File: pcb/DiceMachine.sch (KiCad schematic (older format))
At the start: 12 parts, among them J1 Conn_01x02, J2 Conn_01x02, J3 Conn_01x02, U1 arduino_mini

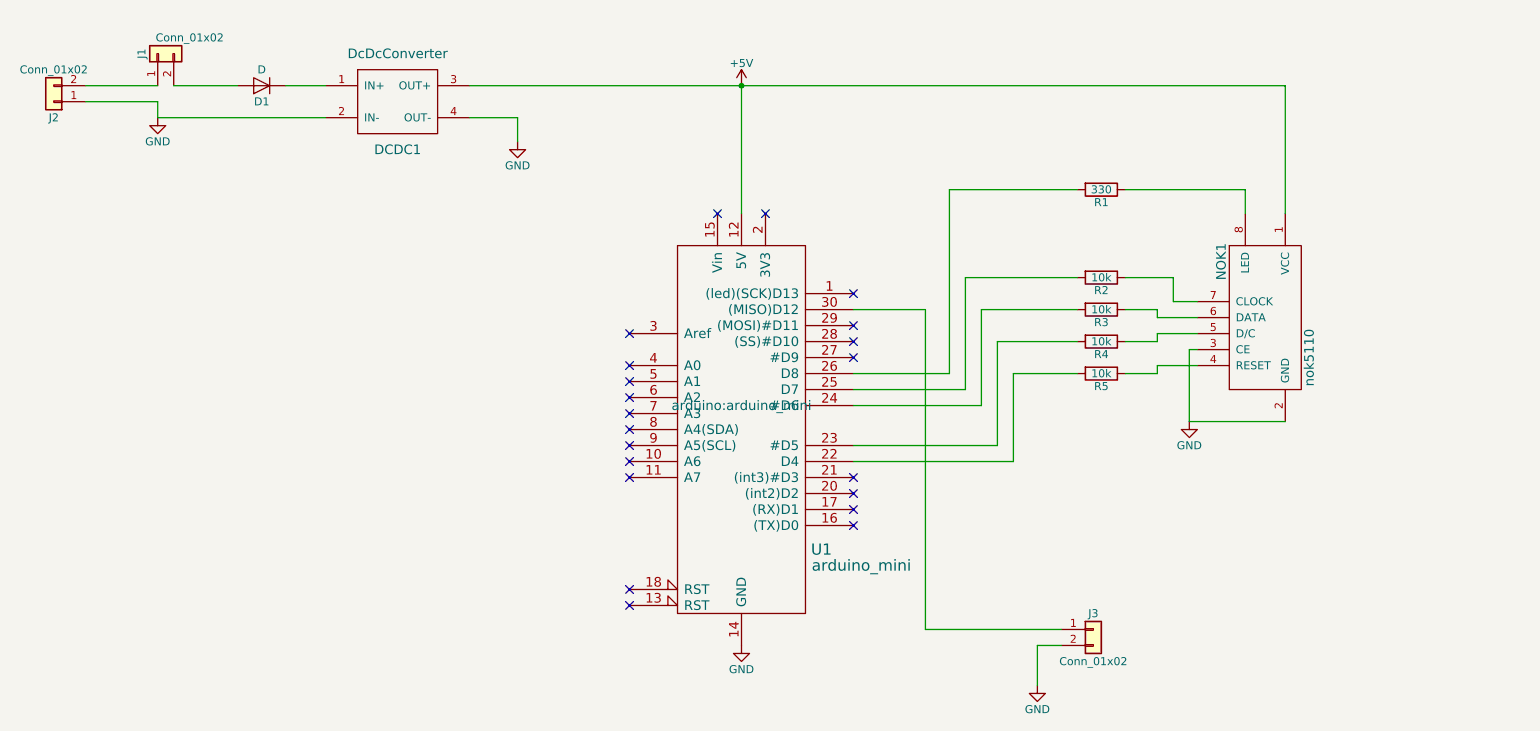
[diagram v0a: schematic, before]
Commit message: added level shifter to PCB
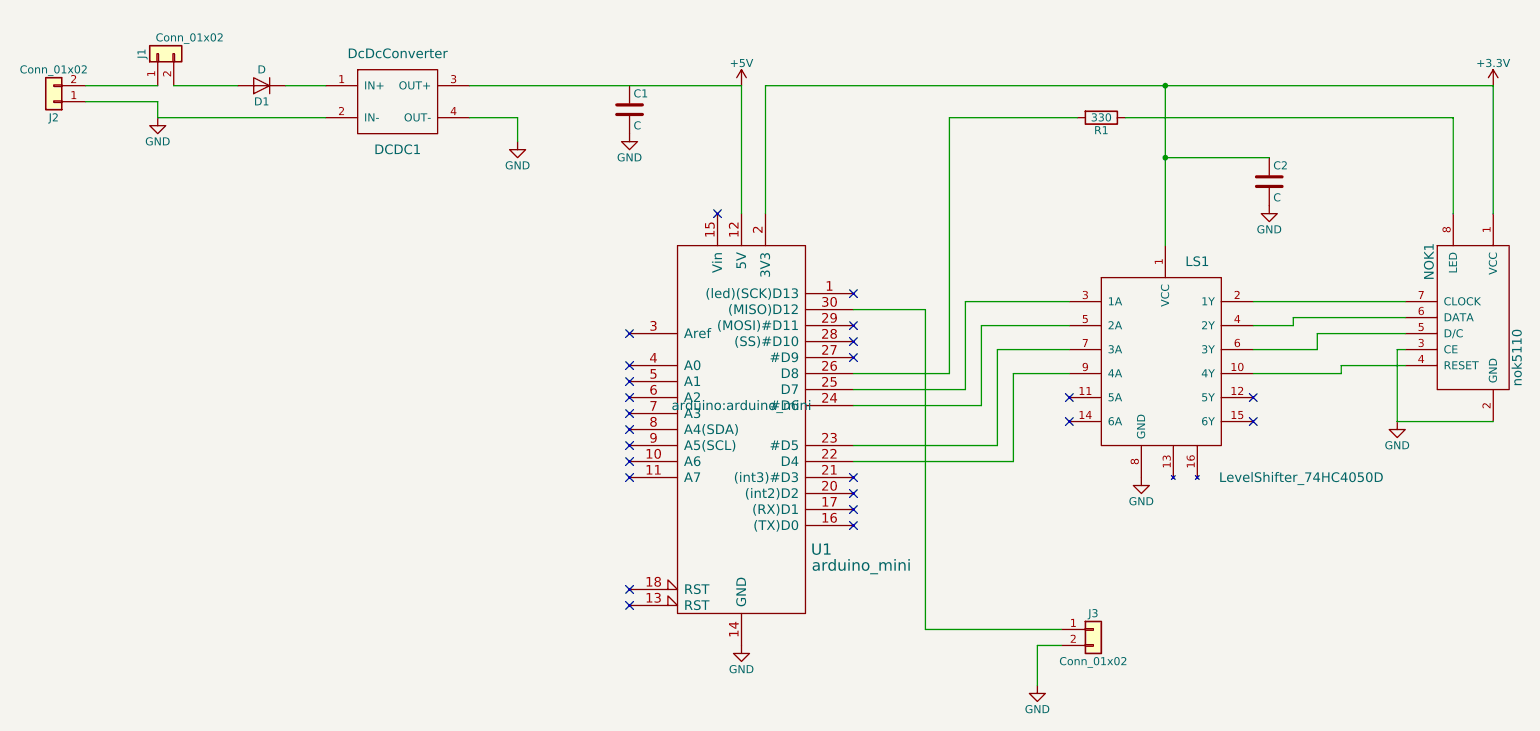
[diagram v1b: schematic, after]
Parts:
- removed R2, R3, R4, R5: 10k, Resistors_ThroughHole:Resistor_Horizontal_RM7mm, symbol R
- added C1, C2: C, Capacitors_SMD:C_1206_HandSoldering, symbol C
- added LS1: LevelShifter_74HC4050D, Housings_SSOP:SOP-16_4.4x10.4mm_Pitch1.27mm, symbol LevelShifter_74HC4050D
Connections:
- net +5V: no longer NOK1.1 (VCC)
- net GND: now also C1.2, C2.2, LS1.8 (GND)
- net +3V3: now reaches U1.2 (3V3)
- net +3V3: now also NOK1.1 (VCC), C2.1, LS1.1 (VCC)
- net at U1.22 (D4): now also LS1.9 (4A)
- net at U1.23 (#D5): now also LS1.7 (3A)
- net at U1.24 (#D6): now also LS1.5 (2A)
- net at U1.25 (D7): now also LS1.3 (1A)
- net at NOK1.7 (CLOCK): now also LS1.2 (1Y)
- net at NOK1.6 (DATA): now also LS1.4 (2Y)
- net at NOK1.5 (D/C): now also LS1.6 (3Y)
- net at NOK1.4 (RESET): now also LS1.10 (4Y)
- no-connect marks 21 -> 24
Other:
- moved on the sheet: NOK1, R1
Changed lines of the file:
@@
 LIBS:arduino
 LIBS:nok5110
+LIBS:levelshifter_74hc4050d
 LIBS:DiceMachine-cache
 EELAYER 25 0
@@
 $EndComp
 $Comp
-L R R2
-U 1 1 59ECDA35
-P 7950 2600
-F 0 "R2" V 8030 2600 50  0000 C CNN
-F 1 "10k" V 7950 2600 50  0000 C CNN
-F 2 "Resistors_ThroughHole:Resistor_Horizontal_RM7mm" V 7880 2600 50  0001 C CNN
-F 3 "" H 7950 2600 50  0001 C CNN
-	1    7950 2600
-	0    1    1    0
-$EndComp
-$Comp
-L R R3
-U 1 1 59ECDAEE
-P 7950 2800
-F 0 "R3" V 8030 2800 50  0000 C CNN
-F 1 "10k" V 7950 2800 50  0000 C CNN
-F 2 "Resistors_ThroughHole:Resistor_Horizontal_RM7mm" V 7880 2800 50  0001 C CNN
-F 3 "" H 7950 2800 50  0001 C CNN
-	1    7950 2800
-	0    1    1    0
-$EndComp
-$Comp
-L R R4
-U 1 1 59ECDC0A
-P 7950 3000
-F 0 "R4" V 8030 3000 50  0000 C CNN
-F 1 "10k" V 7950 3000 50  0000 C CNN
-F 2 "Resistors_ThroughHole:Resistor_Horizontal_RM7mm" V 7880 3000 50  0001 C CNN
-F 3 "" H 7950 3000 50  0001 C CNN
-	1    7950 3000
-	0    1    1    0
-$EndComp
-$Comp
-L R R5
-U 1 1 59ECDC61
-P 7950 3200
-F 0 "R5" V 8030 3200 50  0000 C CNN
-F 1 "10k" V 7950 3200 50  0000 C CNN
-F 2 "Resistors_ThroughHole:Resistor_Horizontal_RM7mm" V 7880 3200 50  0001 C CNN
-F 3 "" H 7950 3200 50  0001 C CNN
-	1    7950 3200
-	0    1    1    0
-$EndComp
-$Comp
 L R R1
 U 1 1 59ECDCA8
-P 7950 2050
-F 0 "R1" V 8030 2050 50  0000 C CNN
-F 1 "330" V 7950 2050 50  0000 C CNN
-F 2 "Resistors_ThroughHole:Resistor_Horizontal_RM7mm" V 7880 2050 50  0001 C CNN
-F 3 "" H 7950 2050 50  0001 C CNN
-	1    7950 2050
+P 7950 1600
+F 0 "R1" V 8030 1600 50  0000 C CNN
+F 1 "330" V 7950 1600 50  0000 C CNN
+F 2 "Resistors_ThroughHole:Resistor_Horizontal_RM7mm" V 7880 1600 50  0001 C CNN
+F 3 "" H 7950 1600 50  0001 C CNN
+	1    7950 1600
 	0    1    1    0
 $EndComp
 Wire Wire Line
-	5700 2200 5700 1400
-Wire Wire Line
-	4000 1400 9100 1400
-Wire Wire Line
-	8850 2050 8850 2200
-Wire Wire Line
-	8100 2600 8400 2600
-Wire Wire Line
-	8400 2600 8400 2750
-Wire Wire Line
-	8400 2750 8550 2750
-Wire Wire Line
-	8300 2850 8550 2850
-Wire Wire Line
-	8300 2950 8550 2950
-Wire Wire Line
-	8550 3050 8500 3050
-Wire Wire Line
-	8500 3050 8500 3500
-Wire Wire Line
-	8500 3500 9100 3500
-$Comp
-L GND #PWR01
+	9850 3050 9800 3050
+Wire Wire Line
+	9800 3050 9800 3500
+Wire Wire Line
+	9800 3500 10400 3500
+$Comp
+L GND #PWR7
 U 1 1 59ECE495
-P 8500 3500
-F 0 "#PWR01" H 8500 3250 50  0001 C CNN
-F 1 "GND" H 8500 3350 50  0000 C CNN
-F 2 "" H 8500 3500 50  0001 C CNN
-F 3 "" H 8500 3500 50  0001 C CNN
-	1    8500 3500
-	1    0    0    -1
-$EndComp
-Wire Wire Line
-	8100 3200 8300 3200
-Wire Wire Line
-	8300 3200 8300 3150
-Wire Wire Line
-	8300 3150 8550 3150
-Wire Wire Line
-	8300 2950 8300 3000
-Wire Wire Line
-	8300 3000 8100 3000
-Wire Wire Line
-	8300 2850 8300 2800
-Wire Wire Line
-	8300 2800 8100 2800
-Wire Wire Line
-	8100 2050 8850 2050
-Wire Wire Line
-	9100 1400 9100 2200
+P 9800 3500
+F 0 "#PWR7" H 9800 3250 50  0001 C CNN
+F 1 "GND" H 9800 3350 50  0000 C CNN
+F 2 "" H 9800 3500 50  0001 C CNN
+F 3 "" H 9800 3500 50  0001 C CNN
+	1    9800 3500
+	1    0    0    -1
+$EndComp
+Wire Wire Line
+	8100 1600 10150 1600
 Wire Wire Line
 	6400 3200 7000 3200
 Wire Wire Line
-	7000 3200 7000 2050
-Wire Wire Line
-	7000 2050 7800 2050
+	7000 3200 7000 1600
+Wire Wire Line
+	7000 1600 7800 1600
 Wire Wire Line
 	6400 3300 7100 3300
 Wire Wire Line
-	7100 3300 7100 2600
-Wire Wire Line
-	7100 2600 7800 2600
+	7100 3300 7100 2750
 Wire Wire Line
 	6400 3400 7200 3400
 Wire Wire Line
-	7200 3400 7200 2800
-Wire Wire Line
-	7200 2800 7800 2800
+	7200 3400 7200 2900
 Wire Wire Line
 	6400 3650 7300 3650
 Wire Wire Line
-	7300 3650 7300 3000
-Wire Wire Line
-	7300 3000 7800 3000
+	7300 3650 7300 3050
 Wire Wire Line
 	6400 3750 7400 3750
@@
 	7400 3750 7400 3200
 Wire Wire Line
-	7400 3200 7800 3200
-Wire Wire Line
 	6400 2800 6850 2800
 Wire Wire Line
@@
 	7550 4900 7550 5150
 $Comp
-L GND #PWR02
+L GND #PWR10
 U 1 1 59ECEB05
 P 7550 5150
-F 0 "#PWR02" H 7550 4900 50  0001 C CNN
+F 0 "#PWR10" H 7550 4900 50  0001 C CNN
 F 1 "GND" H 7550 5000 50  0000 C CNN
 F 2 "" H 7550 5150 50  0001 C CNN
@@
 	1    0    0    -1
 $EndComp
-Connection ~ 5700 1400
 Wire Wire Line
 	4000 1600 4300 1600
@@
 	4300 1600 4300 1750
 $Comp
-L GND #PWR03
+L GND #PWR5
 U 1 1 59ECECE3
 P 4300 1750
-F 0 "#PWR03" H 4300 1500 50  0001 C CNN
+F 0 "#PWR5" H 4300 1500 50  0001 C CNN
 F 1 "GND" H 4300 1600 50  0000 C CNN
 F 2 "" H 4300 1750 50  0001 C CNN
@@
 	2050 1600 3100 1600
 $Comp
-L GND #PWR04
+L GND #PWR9
 U 1 1 59ECEF76
 P 5700 4900
-F 0 "#PWR04" H 5700 4650 50  0001 C CNN
+F 0 "#PWR9" H 5700 4650 50  0001 C CNN
 F 1 "GND" H 5700 4750 50  0000 C CNN
 F 2 "" H 5700 4900 50  0001 C CNN
@@
 NoConn ~ 5000 3850
 NoConn ~ 5550 2200
-NoConn ~ 5850 2200
 $Comp
 L nok5110 NOK1
 U 1 1 59ECF53D
-P 9000 2850
-F 0 "NOK1" V 8700 3200 60  0000 C CNN
-F 1 "nok5110" V 9250 2600 60  0000 C CNN
-F 2 "Pin_Headers:Pin_Header_Straight_1x08" H 8900 3600 60  0001 C CNN
-F 3 "" H 8900 3600 60  0001 C CNN
-	1    9000 2850
-	1    0    0    -1
-$EndComp
-$Comp
-L +5V #PWR?
+P 10300 2850
+F 0 "NOK1" V 10000 3200 60  0000 C CNN
+F 1 "nok5110" V 10550 2600 60  0000 C CNN
+F 2 "Pin_Headers:Pin_Header_Straight_1x08" H 10200 3600 60  0001 C CNN
+F 3 "" H 10200 3600 60  0001 C CNN
+	1    10300 2850
+	1    0    0    -1
+$EndComp
+$Comp
+L +5V #PWR1
 U 1 1 59ECF8EA
 P 5700 1400
-F 0 "#PWR?" H 5700 1250 50  0001 C CNN
+F 0 "#PWR1" H 5700 1250 50  0001 C CNN
 F 1 "+5V" H 5700 1540 50  0000 C CNN
 F 2 "" H 5700 1400 50  0001 C CNN
@@
 $EndComp
 $Comp
-L GND #PWR?
+L GND #PWR3
 U 1 1 59ECFAC3
 P 2050 1600
-F 0 "#PWR?" H 2050 1350 50  0001 C CNN
+F 0 "#PWR3" H 2050 1350 50  0001 C CNN
 F 1 "GND" H 2050 1450 50  0000 C CNN
 F 2 "" H 2050 1600 50  0001 C CNN
@@
 	1    0    0    -1
 $EndComp
+$Comp
+L LevelShifter_74HC4050D LS1
+U 1 1 59FB6E3B
+P 8350 3050
+F 0 "LS1" H 8550 3600 60  0000 C CNN
+F 1 "LevelShifter_74HC4050D" H 9200 2250 60  0000 C CNN
+F 2 "Housings_SSOP:SOP-16_4.4x10.4mm_Pitch1.27mm" H 8350 3050 60  0001 C CNN
+F 3 "" H 8350 3050 60  0000 C CNN
+	1    8350 3050
+	1    0    0    -1
+$EndComp
+Wire Wire Line
+	5700 2200 5700 1400
+Wire Wire Line
+	5700 1400 4000 1400
+Wire Wire Line
+	5850 2200 5850 1400
+Wire Wire Line
+	5850 1400 10400 1400
+Wire Wire Line
+	10400 1400 10400 2200
+$Comp
+L +3.3V #PWR2
+U 1 1 59FB7034
+P 10400 1400
+F 0 "#PWR2" H 10400 1250 50  0001 C CNN
+F 1 "+3.3V" H 10400 1540 50  0000 C CNN
+F 2 "" H 10400 1400 50  0001 C CNN
+F 3 "" H 10400 1400 50  0001 C CNN
+	1    10400 1400
+	1    0    0    -1
+$EndComp
+Wire Wire Line
+	10150 1600 10150 2200
+$Comp
+L GND #PWR8
+U 1 1 59FB736B
+P 8200 3850
+F 0 "#PWR8" H 8200 3600 50  0001 C CNN
+F 1 "GND" H 8200 3700 50  0000 C CNN
+F 2 "" H 8200 3850 50  0001 C CNN
+F 3 "" H 8200 3850 50  0001 C CNN
+	1    8200 3850
+	1    0    0    -1
+$EndComp
+Wire Wire Line
+	8900 2750 9850 2750
+Wire Wire Line
+	7100 2750 7750 2750
+Wire Wire Line
+	7200 2900 7750 2900
+Wire Wire Line
+	8900 2900 9150 2900
+Wire Wire Line
+	9150 2900 9150 2850
+Wire Wire Line
+	9150 2850 9850 2850
+Wire Wire Line
+	7300 3050 7750 3050
+Wire Wire Line
+	8900 3050 9300 3050
+Wire Wire Line
+	9300 3050 9300 2950
+Wire Wire Line
+	9300 2950 9850 2950
+Wire Wire Line
+	7400 3200 7750 3200
+Wire Wire Line
+	8900 3200 9450 3200
+Wire Wire Line
+	9450 3200 9450 3150
+Wire Wire Line
+	9450 3150 9850 3150
+NoConn ~ 8900 3350
+NoConn ~ 8900 3500
+NoConn ~ 7750 3350
+NoConn ~ 7750 3500
+Wire Wire Line
+	8350 2400 8350 1400
+Connection ~ 8350 1400
+$Comp
+L C C2
+U 1 1 59FB7999
+P 9000 2000
+F 0 "C2" H 9025 2100 50  0000 L CNN
+F 1 "C" H 9025 1900 50  0000 L CNN
+F 2 "Capacitors_SMD:C_1206_HandSoldering" H 9038 1850 50  0001 C CNN
+F 3 "" H 9000 2000 50  0001 C CNN
+	1    9000 2000
+	1    0    0    -1
+$EndComp
+$Comp
+L GND #PWR6
+U 1 1 59FB7A2C
+P 9000 2150
+F 0 "#PWR6" H 9000 1900 50  0001 C CNN
+F 1 "GND" H 9000 2000 50  0000 C CNN
+F 2 "" H 9000 2150 50  0001 C CNN
+F 3 "" H 9000 2150 50  0001 C CNN
+	1    9000 2150
+	1    0    0    -1
+$EndComp
+Wire Wire Line
+	9000 1850 8350 1850
+Connection ~ 8350 1850
+$Comp
+L C C1
+U 1 1 59FB7B51
+P 5000 1550
+F 0 "C1" H 5025 1650 50  0000 L CNN
+F 1 "C" H 5025 1450 50  0000 L CNN
+F 2 "Capacitors_SMD:C_1206_HandSoldering" H 5038 1400 50  0001 C CNN
+F 3 "" H 5000 1550 50  0001 C CNN
+	1    5000 1550
+	1    0    0    -1
+$EndComp
+$Comp
+L GND #PWR4
+U 1 1 59FB7BA4
+P 5000 1700
+F 0 "#PWR4" H 5000 1450 50  0001 C CNN
+F 1 "GND" H 5000 1550 50  0000 C CNN
+F 2 "" H 5000 1700 50  0001 C CNN
+F 3 "" H 5000 1700 50  0001 C CNN
+	1    5000 1700
+	1    0    0    -1
+$EndComp

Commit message: Schema image
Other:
- note added: "Button"
- note added: "Power input"
- note added: "Power switch"
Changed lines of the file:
@@
 P 2050 1200
 F 0 "J1" H 2050 1300 50  0000 C CNN
-F 1 "Conn_01x02" V 2150 1000 50  0000 C CNN
+F 1 "Conn_01x02" V 2150 1150 50  0000 C CNN
 F 2 "Pin_Headers:Pin_Header_Straight_1x02" H 2050 1200 50  0001 C CNN
 F 3 "" H 2050 1200 50  0001 C CNN
@@
 	1    0    0    -1
 $EndComp
+Text Notes 1150 1250 0    60   ~ 0
+Power input
+Text Notes 1800 1050 0    60   ~ 0
+Power switch
+Text Notes 7800 4650 0    60   ~ 0
+Button
 $EndSCHEMATC
